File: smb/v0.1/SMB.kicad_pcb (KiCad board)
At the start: 2 copper layers, 99 parts, among them IC1 MAX485, IC101 ATMEGA1284-A, IC2 DS2482-100S, J101 RJ45, J102 RTS_RESET, J103 ICSP, J104 SERIAL_REV, J202 USD_CONN, J401 HR911105_RJ45, P1 CONN_2, P101 I2C_CONN, P102 CONN_10X2, P103 CONN_5, P105 CONN_5, P107 CONN_3, P108 CONN_5, P109 CONN_3, P110 CONN_3, P112 CONN_3, P2 CONN_3, P301 CONN_2, SW101 SKQGAKE010, U201 ENC28J60, U202 LM1117IMP-3.3, U301 74HC08, U302 MP2562DS, U303 74HC08, X101 20MHz, X201 25MHz

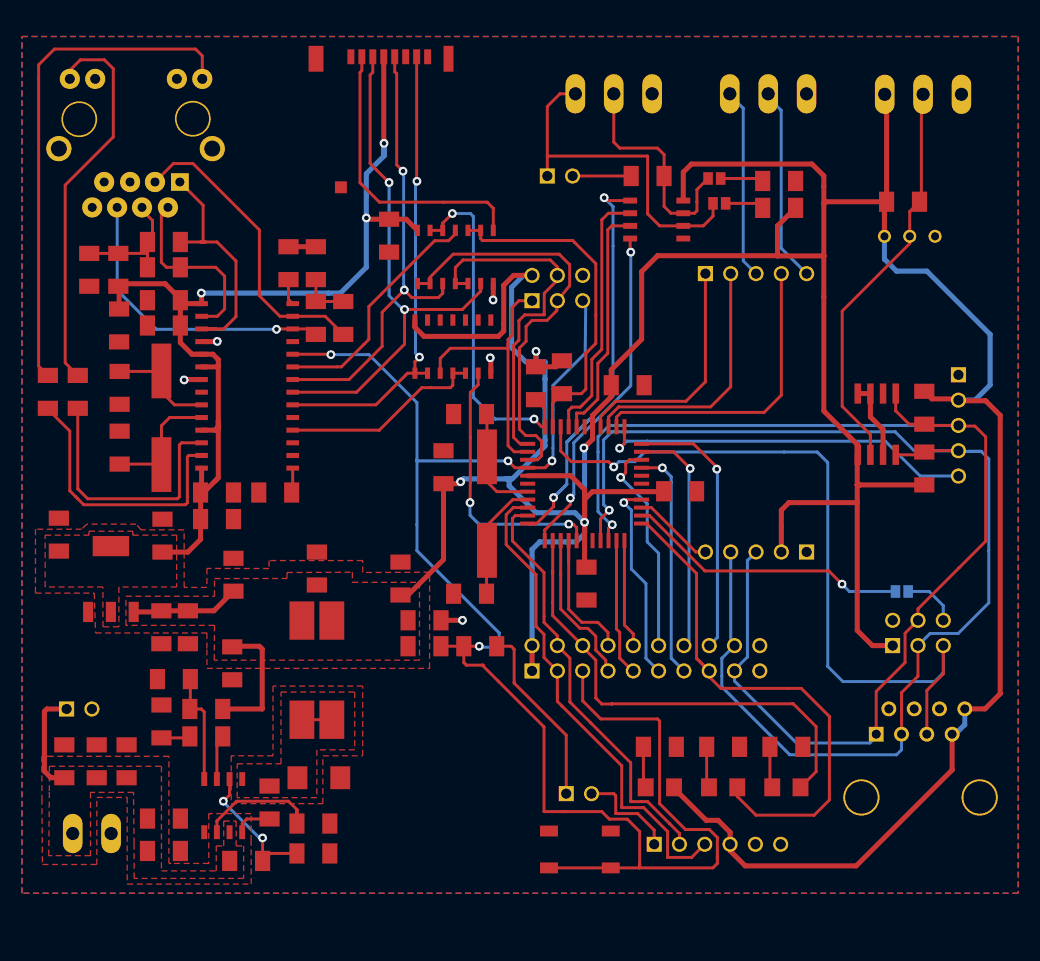
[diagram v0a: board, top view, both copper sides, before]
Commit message: ajout percage rj45 i2c (blindage) retouche routage
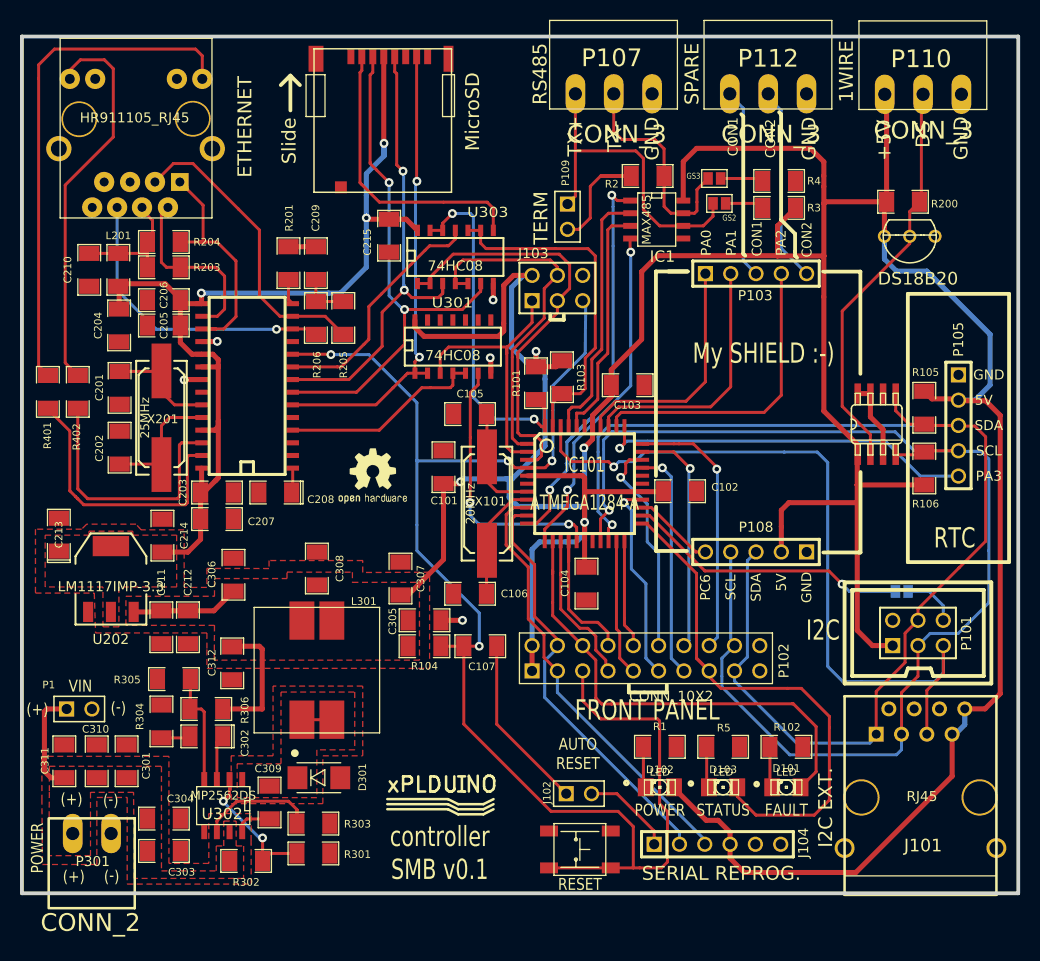
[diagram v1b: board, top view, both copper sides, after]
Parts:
- moved P109 4.15 mm to (87.8, 45.1), turned to 270 degrees
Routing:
- net /RESET: track 163.2 -> 148.8 mm
- net N-0000021: track 5.88 -> 13.5 mm
- net RX0: track 49.1 -> 43.8 mm
- net +5V: track 417.4 -> 421.0 mm
- net RX1: track 47.5 -> 44.9 mm
- net ETH_CS_33: track 24.1 -> 26.2 mm
- net TX+: track 34.9 -> 33.0 mm
- net N-000008: track 10.3 -> 9.17 mm
- net SPI_MOSI: track 37.1 -> 36.2 mm
- net N-000009: track 18.5 -> 17.7 mm
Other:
- board outline added: 100 x 86 mm
